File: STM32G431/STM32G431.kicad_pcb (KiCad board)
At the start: 4 copper layers, 60 x 44 mm, 156 parts, among them J1 W, J10 NTC, J11 LED, J2 U, J3 V, J4 GND, J5 VIN, J6 UART, J8 HALL, J9 AIN/PWM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

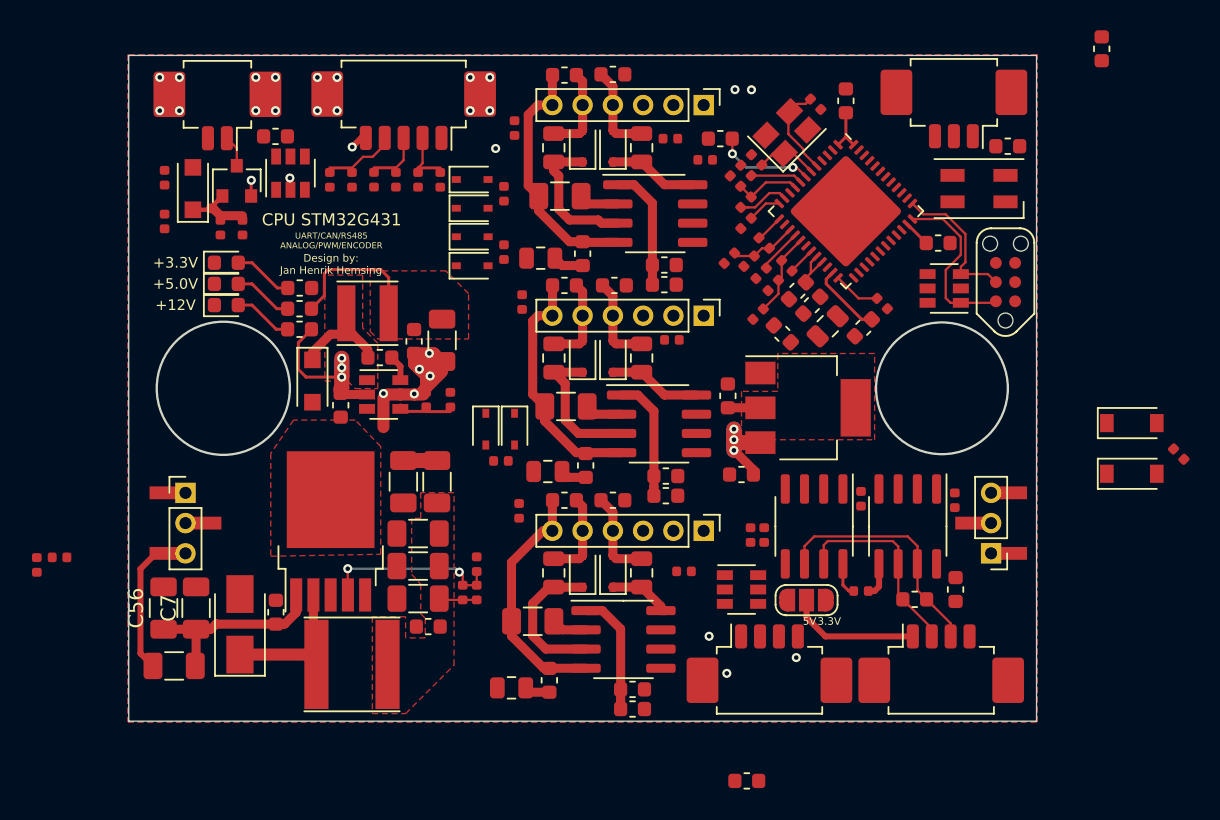
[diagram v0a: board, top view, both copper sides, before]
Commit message: updated layout
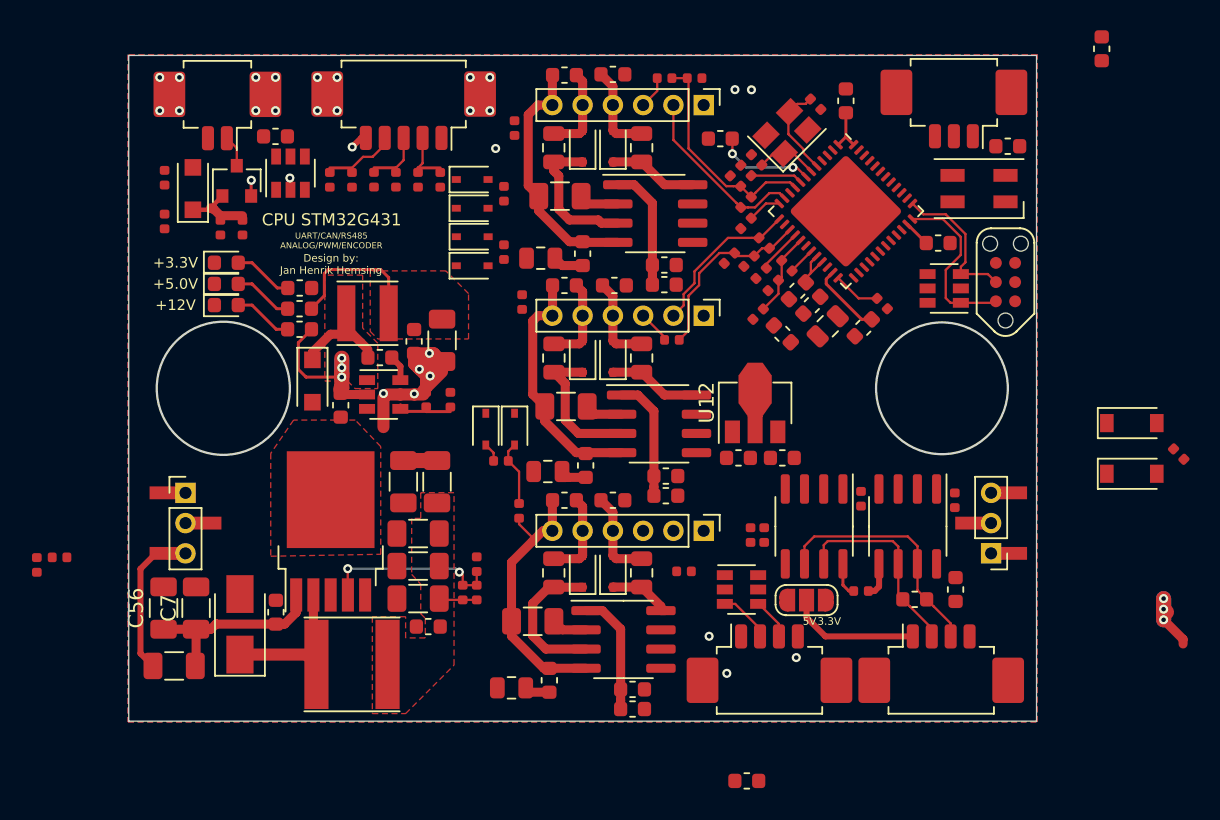
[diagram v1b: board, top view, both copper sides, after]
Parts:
- U12: value AMS1117-3.3 -> AP2204R-3.3; footprint Package_TO_SOT_SMD:SOT-223-3_TabPin2 -> Package_TO_SOT_SMD:SOT-89-3
- moved C46 5.46 mm to (63.2, 49.6), turned to 180 degrees
- moved R16 5.45 mm to (57.4, 24.5)
- moved R42 4.02 mm to (55.4, 24.5)
- moved U12 3.50 mm to (61.4, 46.4), turned to 90 degrees
- moved C43 1.12 mm to (60.3, 49.6), turned to 0 degrees
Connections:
- U12 pad 1: GND -> +12V
- U12 pad 2: +3V3 -> GND
- U12 pad 3: +12V -> +3V3
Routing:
- net IWH: track 4.46 -> 14.6 mm
- net IVL: track 1.86 -> 10.5 mm
- net IWL: track 3.43 -> 12.0 mm
- net IVH: track 4.46 -> 12.3 mm
- net UU: track 3.13 -> 7.46 mm
- net PWM: track 0.00 -> 3.51 mm
- net AinC: track 0.00 -> 2.75 mm
- net Net-(J3-Pad3): track 0.00 -> 2.19 mm
- net Net-(J1-Pad3): track 0.00 -> 2.17 mm
- net +3V3: track 11.9 -> 9.73 mm
- net U: track 16.3 -> 18.2 mm
- net +12V: track 45.6 -> 44.1 mm
- net Net-(D5-Pad2): track 0.00 -> 1.26 mm
- removed copper zone on F.Cu, net +3V3

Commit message: updated layout
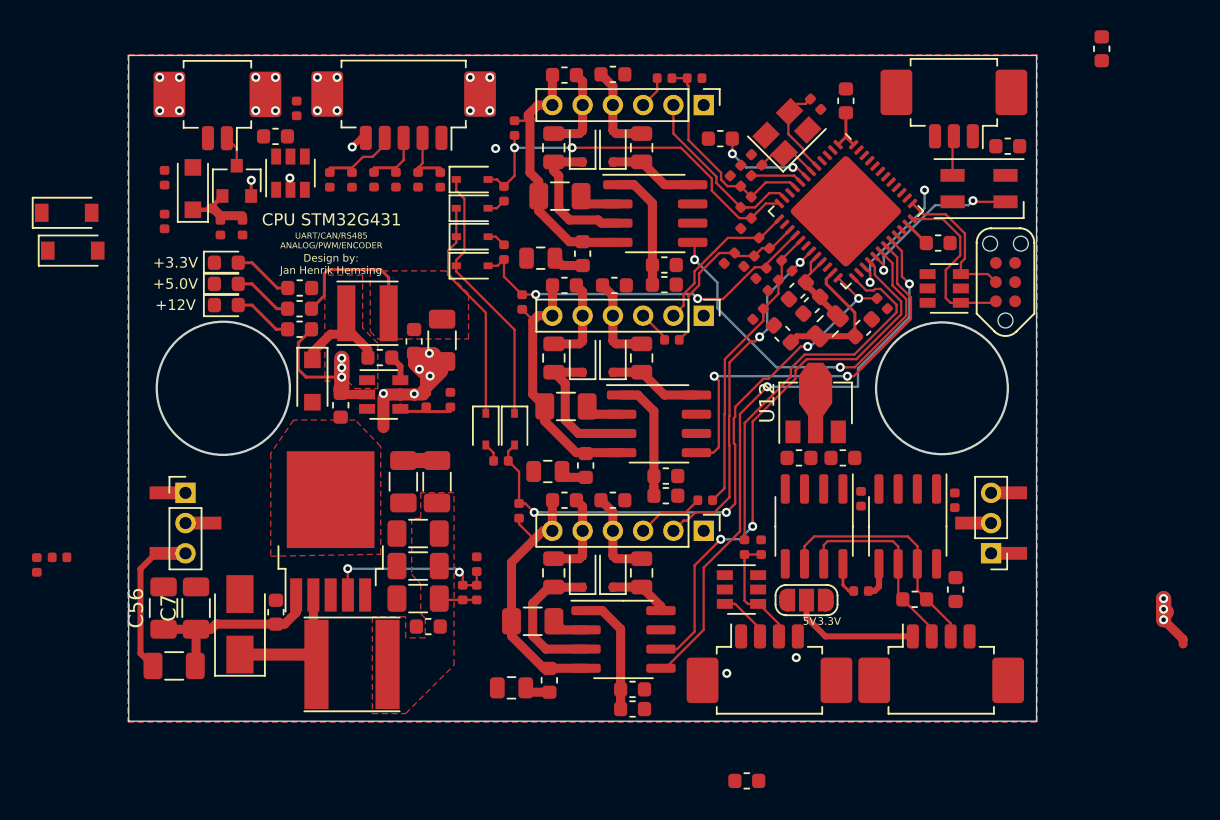
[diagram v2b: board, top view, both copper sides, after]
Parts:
- moved D15 72.5 mm to (15.9, 33.4)
- moved D14 70.9 mm to (16.3, 35.9)
- moved R39 62.6 mm to (31.1, 26.5), turned to 270 degrees
- moved R40 4.90 mm to (58.1, 52.4)
- moved U12 4.00 mm to (65.4, 46.4)
- moved C43 4.00 mm to (64.3, 49.6)
- moved C46 4.00 mm to (67.2, 49.6)
- moved R45 0.89 mm to (60.7, 55.5)
- moved R46 0.82 mm to (61.8, 55.5), turned to 270 degrees
- turned C8 to 45 degrees
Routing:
- net UH: track 0.00 -> 39.3 mm, vias 0 -> 2
- net UL: track 0.00 -> 36.3 mm, vias 0 -> 2
- net UU: track 7.46 -> 39.8 mm, vias 0 -> 4
- net VH: track 0.05 -> 26.6 mm, vias 0 -> 2
- net WH: track 0.00 -> 25.5 mm, vias 0 -> 2
- net Ain: track 0.00 -> 25.3 mm
- net UW: track 2.26 -> 25.2 mm, vias 0 -> 2
- net IUL: track 1.84 -> 24.1 mm, vias 0 -> 2
- net +3V3: track 9.73 -> 31.9 mm
- net UV: track 2.98 -> 24.2 mm, vias 0 -> 2
- net GPIO_BEMF: track 0.00 -> 14.8 mm
- net IUH: track 5.55 -> 19.6 mm
- net SK6812: track 0.00 -> 12.0 mm, vias 0 -> 2
- net NTC_IO: track 0.00 -> 8.71 mm, vias 0 -> 2
- net AinC: track 2.75 -> 7.89 mm
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
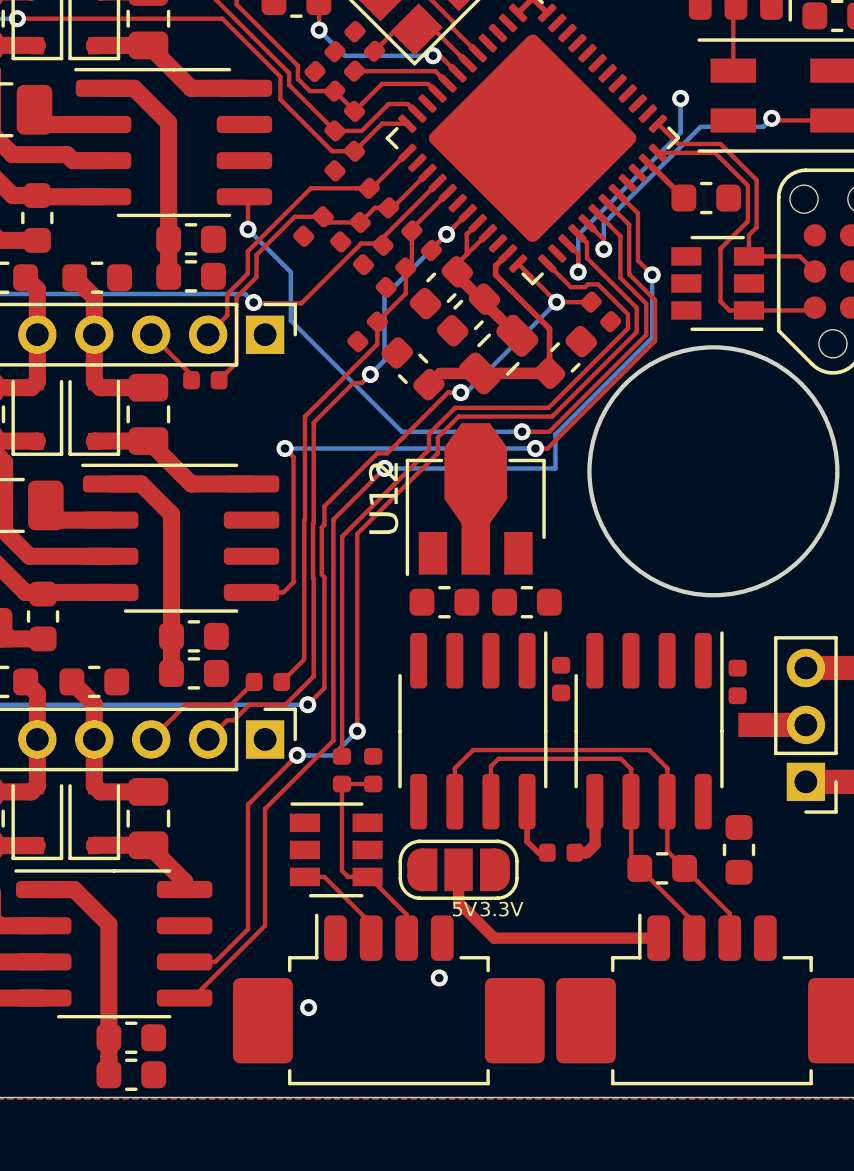
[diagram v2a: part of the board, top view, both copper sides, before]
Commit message: updated layout
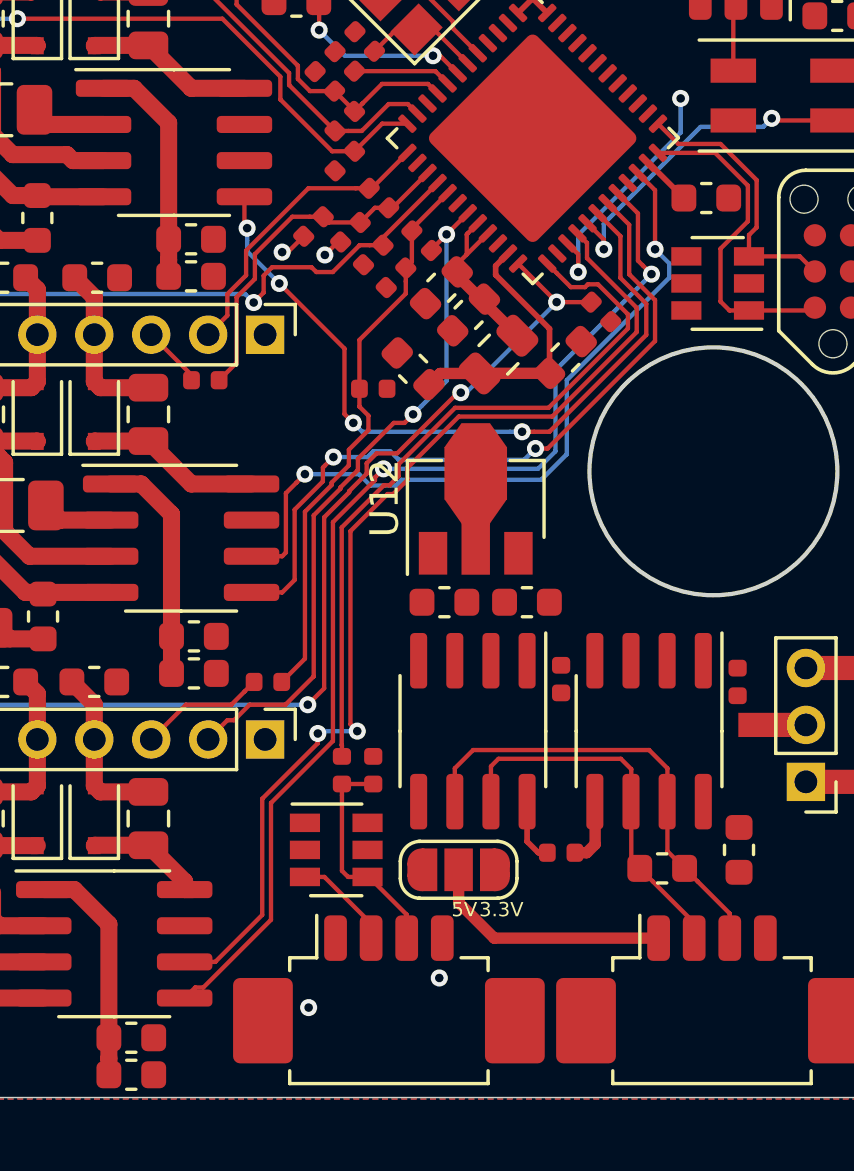
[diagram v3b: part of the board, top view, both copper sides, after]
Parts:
- moved R8 2.01 mm to (61.8, 42.1), turned to 0 degrees
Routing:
- net VL: track 0.00 -> 25.9 mm, vias 0 -> 2
- net VH: track 26.6 -> 25.4 mm
- net +3V3: track 31.9 -> 32.9 mm, vias 0 -> 1
- net WH: track 25.5 -> 26.3 mm, vias 2 -> 4
- net GND: track 26.7 -> 27.5 mm, vias 27 -> 28

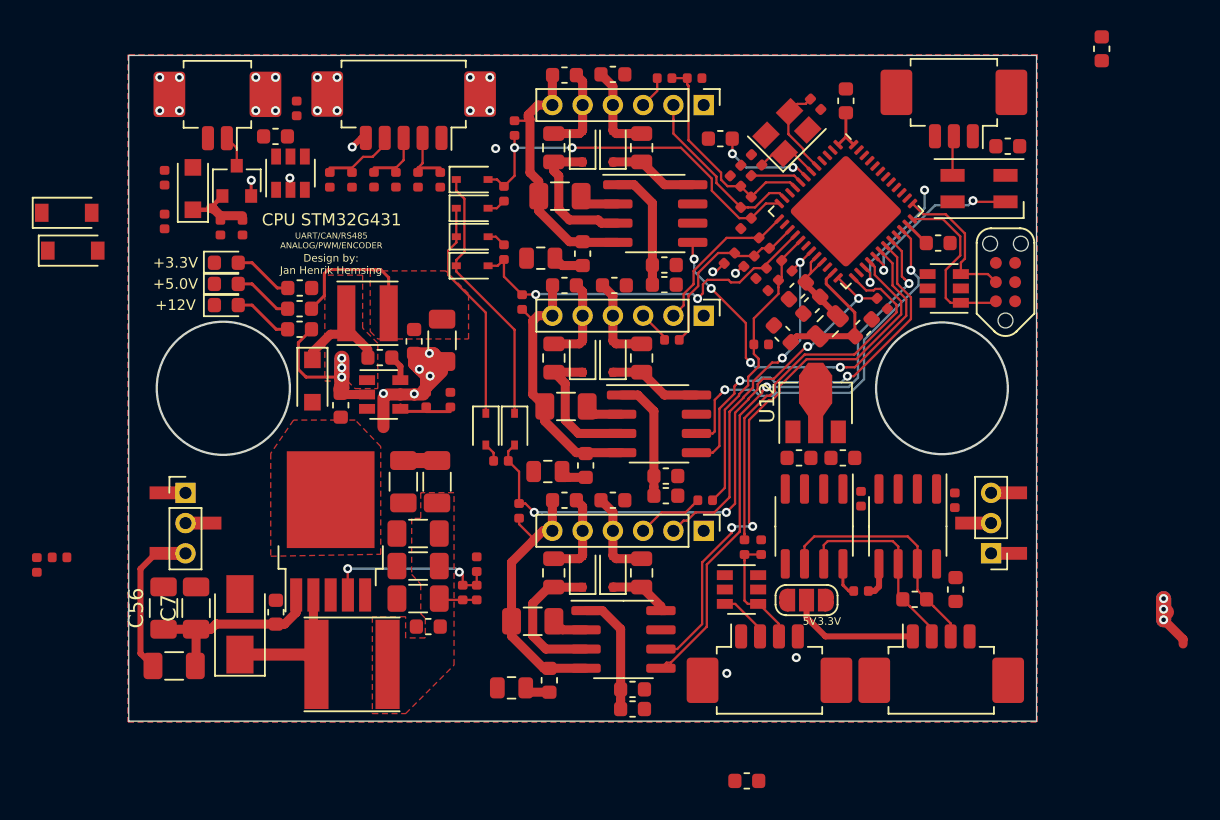
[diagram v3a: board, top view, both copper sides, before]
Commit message: updated layout
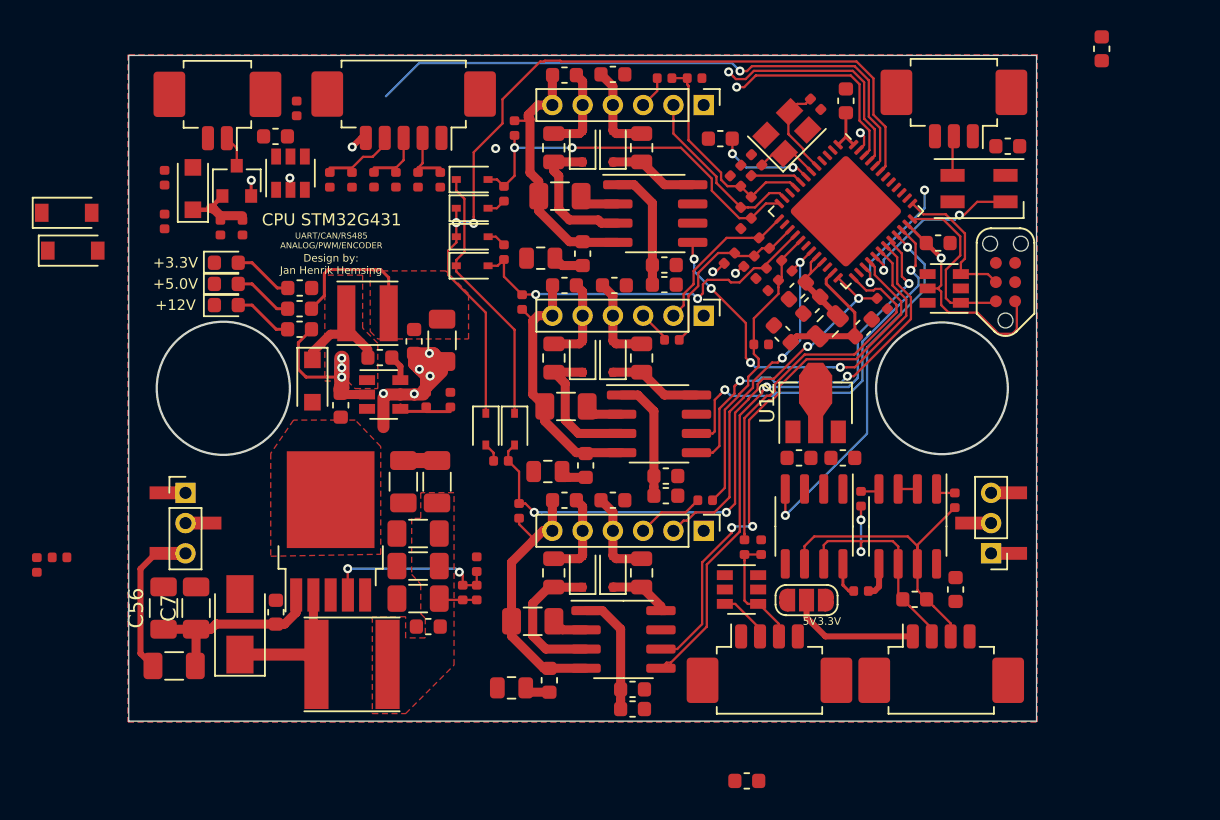
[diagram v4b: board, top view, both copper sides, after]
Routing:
- net GPIO_BEMF: track 14.8 -> 57.6 mm, vias 0 -> 2
- net HALL3: track 0.00 -> 39.7 mm, vias 0 -> 1
- net CANRX: track 0.00 -> 24.9 mm, vias 0 -> 2
- net HALL2: track 0.00 -> 15.3 mm, vias 0 -> 1
- net HALL1: track 0.00 -> 13.8 mm, vias 0 -> 1
- net +3V3: track 32.9 -> 46.1 mm, vias 1 -> 2
- net +12V: track 44.1 -> 38.9 mm, vias 6 -> 3
- net CANL: track 15.4 -> 20.2 mm
- net CANH: track 13.2 -> 17.0 mm, vias 0 -> 2
- net CANTX: track 0.00 -> 1.38 mm, vias 0 -> 1
- net UART_TX: track 0.00 -> 1.31 mm
- net RS485RXTX: track 0.00 -> 1.27 mm
- net UART_RX: track 0.00 -> 1.25 mm
- net GND: vias 28 -> 10

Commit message: updated layout
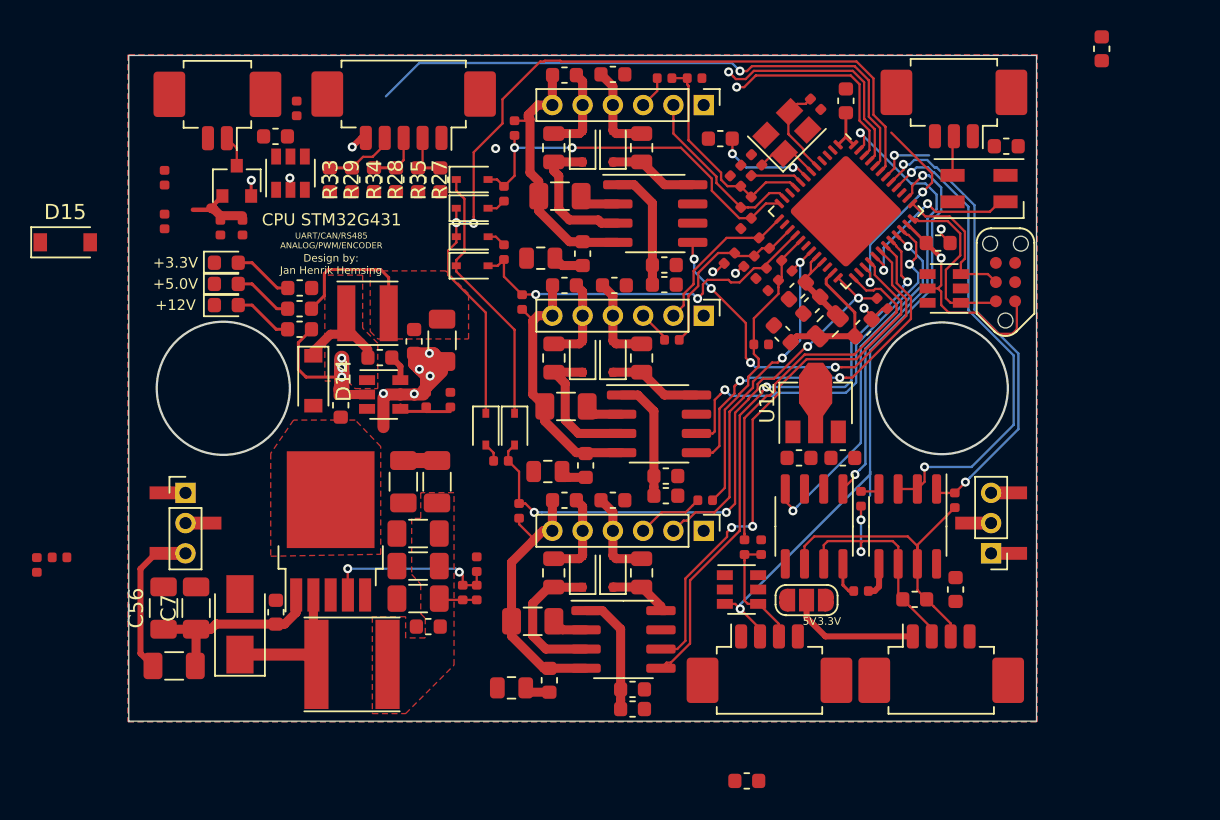
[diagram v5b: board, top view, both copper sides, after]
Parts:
- removed the D14 at (16.3, 35.9)
- removed the D14 at (32.1, 44.5)
- removed the D15 at (15.9, 33.4)
- removed the D15 at (24.2, 31.8)
- added D14: B5819W, Diode_SMD:D_SOD-123, F.Cu at (32.2, 44.5)
- added D15: B5819W, Diode_SMD:D_SOD-123, F.Cu at (15.8, 35.4)
- R27, R28, R29, R33, R34, R35: footprint Resistor_SMD:R_0402_1005Metric -> Resistor_SMD:R_0603_1608Metric
- moved C55 0.10 mm to (78.0, 29.0), turned to 180 degrees
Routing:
- net PWM: track 3.51 -> 42.0 mm, vias 0 -> 2
- net RS485RXTX: track 1.27 -> 32.0 mm, vias 0 -> 2
- net UART_TX: track 1.31 -> 30.8 mm, vias 0 -> 2
- net CANTX: track 1.38 -> 30.1 mm, vias 1 -> 2
- net NTC_IO: track 8.71 -> 13.8 mm
- net UART_RX: track 1.25 -> 5.21 mm, vias 0 -> 1
- net GND: track 27.5 -> 30.9 mm, vias 10 -> 12
- net CANRX: track 24.9 -> 24.2 mm
- net SK6812: track 11.9 -> 12.4 mm
